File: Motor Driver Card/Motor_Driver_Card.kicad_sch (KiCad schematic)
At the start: 1 part

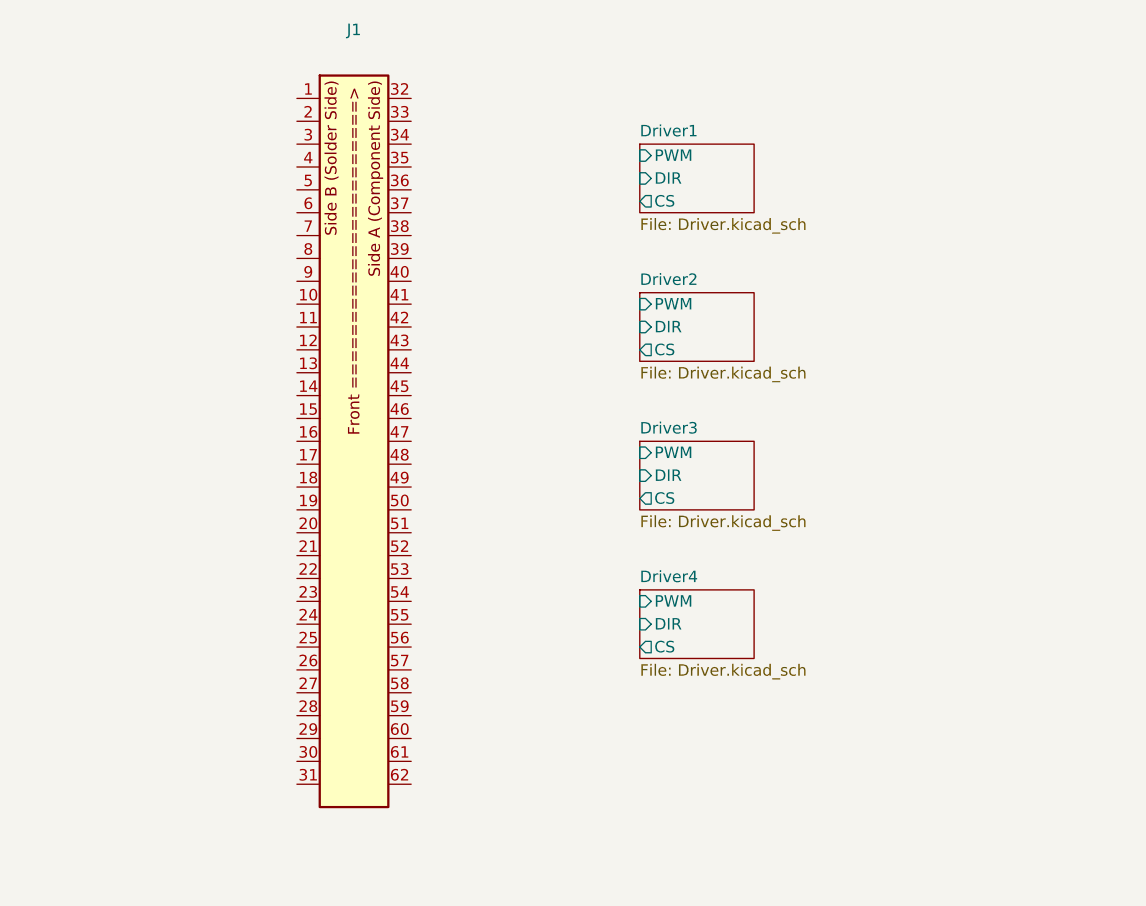
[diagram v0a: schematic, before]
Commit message: Route motor driver card
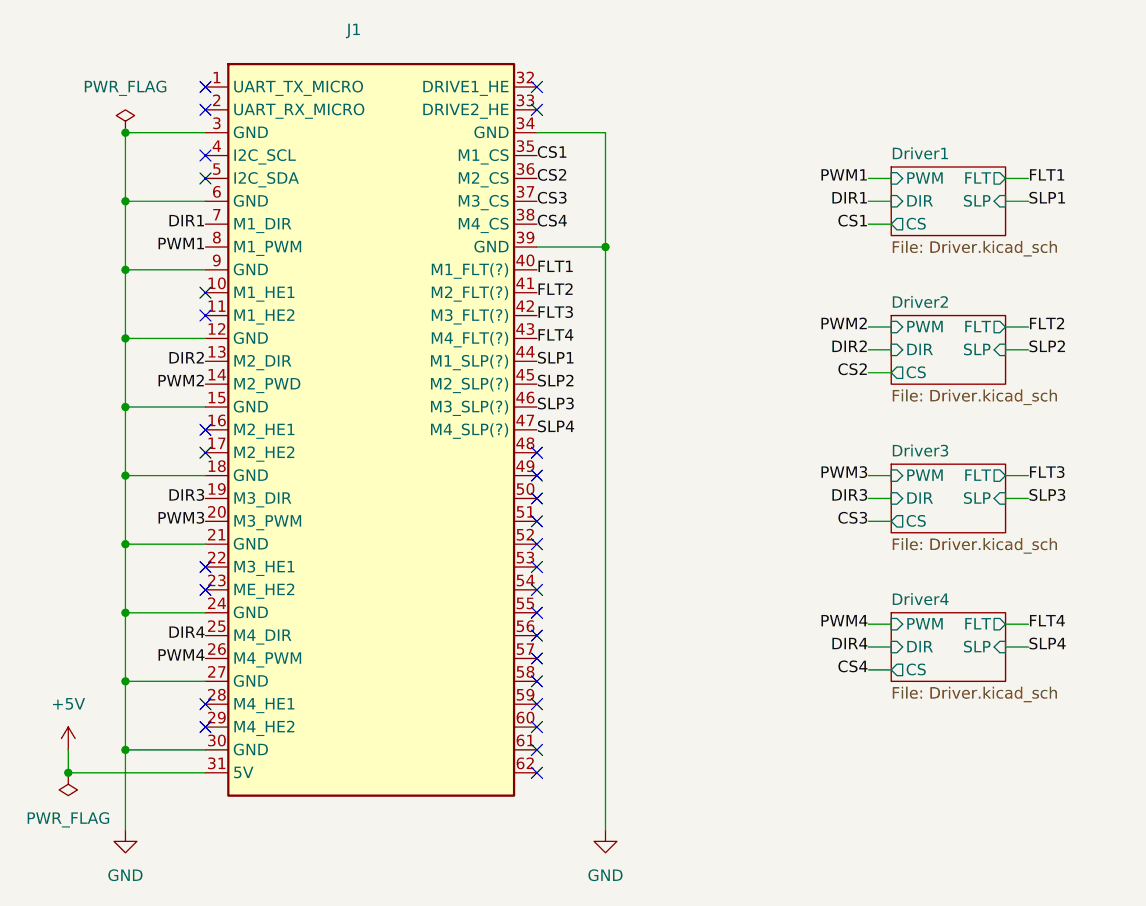
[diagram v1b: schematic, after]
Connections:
- net GND: now reaches J1.12 (GND)
- net GND: now also J1.15 (GND), J1.18 (GND), J1.21 (GND), J1.24 (GND), J1.27 (GND), J1.3 (GND), J1.30 (GND), J1.34 (GND), J1.39 (GND), J1.6 (GND), J1.9 (GND)
- net DIR2: now reaches J1.13 (M2_DIR)
- net PWM2: now reaches J1.14 (M2_PWD)
- net DIR3: now reaches J1.19 (M3_DIR)
- net PWM3: now reaches J1.20 (M3_PWM)
- net DIR4: now reaches J1.25 (M4_DIR)
- net PWM4: now reaches J1.26 (M4_PWM)
- net +5V: now reaches J1.31 (5V)
- net CS1: now reaches J1.35 (M1_CS)
- net CS2: now reaches J1.36 (M2_CS)
- net CS3: now reaches J1.37 (M3_CS)
- net CS4: now reaches J1.38 (M4_CS)
- net FLT1: now reaches J1.40 (M1_FLT(?))
- net FLT2: now reaches J1.41 (M2_FLT(?))
- net FLT3: now reaches J1.42 (M3_FLT(?))
- net FLT4: now reaches J1.43 (M4_FLT(?))
- net SLP1: now reaches J1.44 (M1_SLP(?))
- net SLP2: now reaches J1.45 (M2_SLP(?))
- net SLP3: now reaches J1.46 (M3_SLP(?))
- net SLP4: now reaches J1.47 (M4_SLP(?))
- net DIR1: now reaches J1.7 (M1_DIR)
- net PWM1: now reaches J1.8 (M1_PWM)
- no-connect marks 0 -> 29
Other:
- sheet Driver1 ports: added FLT, SLP; removed none
- sheet Driver2 ports: added FLT, SLP; removed none
- sheet Driver3 ports: added FLT, SLP; removed none
- sheet Driver4 ports: added FLT, SLP; removed none

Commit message: Apply new backplane pinouts to motor driver card
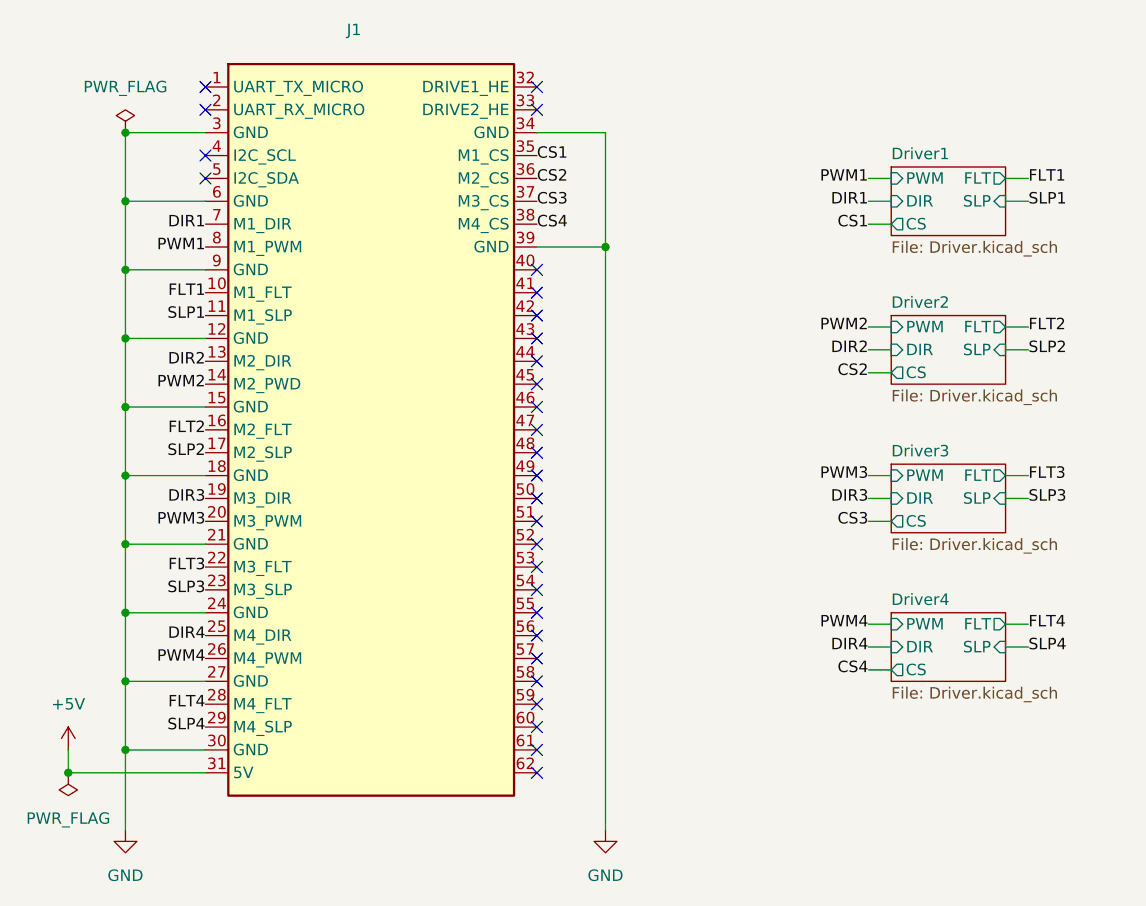
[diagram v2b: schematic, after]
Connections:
- net FLT1: now also J1.10 (M1_FLT); no longer J1.40 (M1_FLT(?))
- net FLT2: now also J1.16 (M2_FLT); no longer J1.41 (M2_FLT(?))
- net FLT3: now also J1.22 (M3_FLT); no longer J1.42 (M3_FLT(?))
- net FLT4: now also J1.28 (M4_FLT); no longer J1.43 (M4_FLT(?))
- net SLP1: now also J1.11 (M1_SLP); no longer J1.44 (M1_SLP(?))
- net SLP2: now also J1.17 (M2_SLP); no longer J1.45 (M2_SLP(?))
- net SLP3: now also J1.23 (M3_SLP); no longer J1.46 (M3_SLP(?))
- net SLP4: now also J1.29 (M4_SLP); no longer J1.47 (M4_SLP(?))
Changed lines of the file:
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@@
-	)
-	(no_connect
-		(at 106.68 74.93)
 	)
 	(no_connect
@@
 	)
 	(no_connect
-		(at 106.68 123.19)
+		(at 143.51 87.63)
 	)
 	(no_connect
@@
 	)
 	(no_connect
-		(at 106.68 120.65)
+		(at 143.51 72.39)
+	)
+	(no_connect
+		(at 143.51 90.17)
 	)
 	(no_connect
@@
 	)
 	(no_connect
-		(at 106.68 105.41)
+		(at 143.51 77.47)
+	)
+	(no_connect
+		(at 143.51 85.09)
 	)
 	(no_connect
@@
 	)
 	(no_connect
-		(at 106.68 90.17)
-	)
-	(no_connect
-		(at 106.68 92.71)
+		(at 143.51 82.55)
 	)
 	(no_connect
@@
 	)
 	(no_connect
-		(at 106.68 77.47)
+		(at 143.51 74.93)
 	)
 	(no_connect
@@
 	)
 	(no_connect
-		(at 106.68 107.95)
-	)
-	(no_connect
 		(at 143.51 92.71)
 	)
@@
 	(no_connect
 		(at 143.51 113.03)
+	)
+	(no_connect
+		(at 143.51 80.01)
 	)
 	(wire
@@
 	)
 	(label "FLT3"
-		(at 143.51 77.47 0)
-		(effects
-			(font
-				(size 1.27 1.27)
-			)
-			(justify left)
+		(at 106.68 105.41 180)
+		(effects
+			(font
+				(size 1.27 1.27)
+			)
+			(justify right)
 		)
 	)
 	(label "SLP2"
-		(at 143.51 85.09 0)
-		(effects
-			(font
-				(size 1.27 1.27)
-			)
-			(justify left)
+		(at 106.68 92.71 180)
+		(effects
+			(font
+				(size 1.27 1.27)
+			)
+			(justify right)
 		)
 	)
@@
 	)
 	(label "FLT4"
-		(at 143.51 80.01 0)
-		(effects
-			(font
-				(size 1.27 1.27)
-			)
-			(justify left)
+		(at 106.68 120.65 180)
+		(effects
+			(font
+				(size 1.27 1.27)
+			)
+			(justify right)
 		)
 	)
@@
 	)
 	(label "FLT1"
-		(at 143.51 72.39 0)
-		(effects
-			(font
-				(size 1.27 1.27)
-			)
-			(justify left)
+		(at 106.68 74.93 180)
+		(effects
+			(font
+				(size 1.27 1.27)
+			)
+			(justify right)
 		)
 	)
@@
 	)
 	(label "SLP3"
-		(at 143.51 87.63 0)
-		(effects
-			(font
-				(size 1.27 1.27)
-			)
-			(justify left)
+		(at 106.68 107.95 180)
+		(effects
+			(font
+				(size 1.27 1.27)
+			)
+			(justify right)
 		)
 	)
@@
 	)
 	(label "FLT2"
-		(at 143.51 74.93 0)
-		(effects
-			(font
-				(size 1.27 1.27)
-			)
-			(justify left)
+		(at 106.68 90.17 180)
+		(effects
+			(font
+				(size 1.27 1.27)
+			)
+			(justify right)
 		)
 	)
@@
 	)
 	(label "SLP1"
-		(at 143.51 82.55 0)
-		(effects
-			(font
-				(size 1.27 1.27)
-			)
-			(justify left)
+		(at 106.68 77.47 180)
+		(effects
+			(font
+				(size 1.27 1.27)
+			)
+			(justify right)
 		)
 	)
@@
 	)
 	(label "SLP4"
-		(at 143.51 90.17 0)
-		(effects
-			(font
-				(size 1.27 1.27)
-			)
-			(justify left)
-		)
-	)
+		(at 106.68 123.19 180)
+		(effects
+			(font
+				(size 1.27 1.27)
+			)
+			(justify right)
+		)
+	)

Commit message: Last-minute changes for pico GPIO voltage levels
Adjusted MDCB to work in 3.3v rather than 5v to not blow up a pico. Thankfully we have a readily available 3.3v source from the motor drivers themselves.
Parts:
- J1: value ~ -> (none)
